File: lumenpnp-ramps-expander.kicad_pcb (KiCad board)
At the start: 2 copper layers, 53 x 98 mm, 70 parts, among them J1 12/24V, J10 A_MICROSTEPS, J11 A_DIAG, J12 A_VDD, J13 DIAG, J14 B_MICROSTEPS, J15 A_DIAG, J16 B_VDD, J2 EXP1, J3 EXP2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

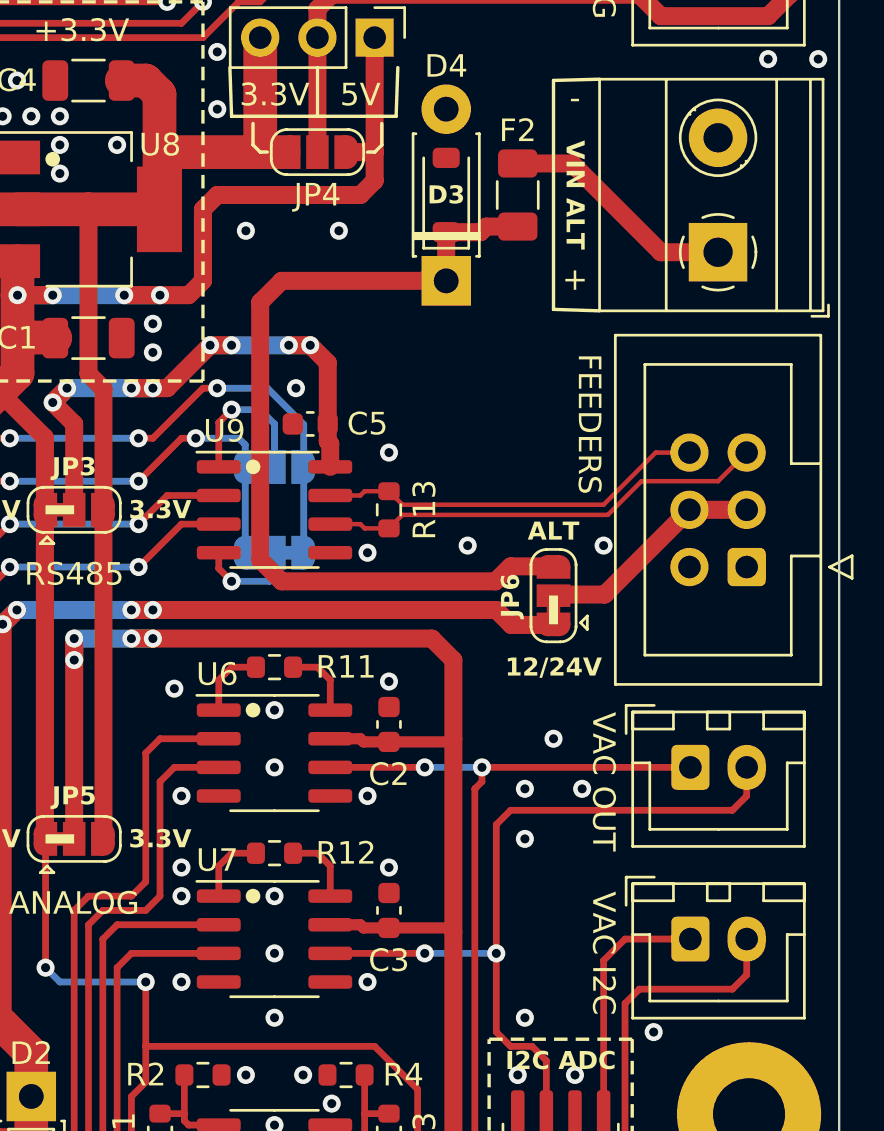
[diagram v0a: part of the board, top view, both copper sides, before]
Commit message: Add NIS4461 efuse for feeder power
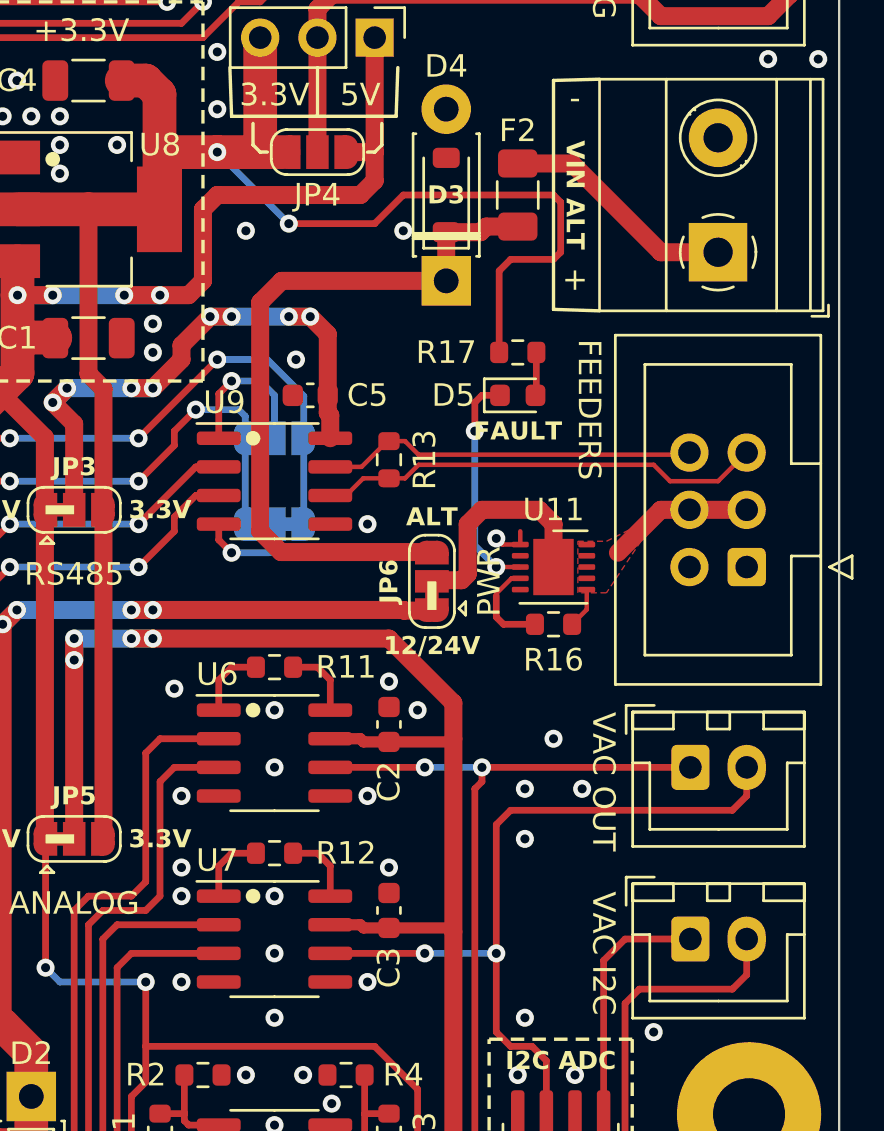
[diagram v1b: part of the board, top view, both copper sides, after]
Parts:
- added D5: FAULT, LED_SMD:LED_0603_1608Metric, F.Cu at (-31.3, 50.6)
- added R16: 20, Resistor_SMD:R_0603_1608Metric, F.Cu at (-29.7, 60.8)
- added R17: 470, Resistor_SMD:R_0603_1608Metric, F.Cu at (-31.3, 48.7)
- added U11: NIS4461, Package_DFN_QFN:WDFN-10-1EP_3x3mm_P0.5mm_EP1.8x2.5mm, F.Cu at (-29.7, 58.2)
- moved JP6 5.43 mm to (-35.1, 58.9)
- moved R13 2.22 mm to (-37.0, 53.5)
- moved C5 1.27 mm to (-40.5, 50.6)
- moved JP1 1.27 mm to (-42.1, 52.5)
- moved JP2 1.27 mm to (-42.1, 56.3)
- moved U9 1.27 mm to (-42.1, 54.4)
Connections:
- J7 pad 3: /VCC_FEEDERS -> Net-(J7-Pin_3)
- J7 pad 4: /VCC_FEEDERS -> Net-(J7-Pin_3)
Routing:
- net +3.3V: track 52.1 -> 78.2 mm, vias 0 -> 2
- net Net-(D5-K): track 0.00 -> 10.0 mm, vias 0 -> 2
- net Net-(J7-Pin_3): track 0.00 -> 8.31 mm
- net /VIN_ALT_FEEDERS: track 39.2 -> 32.3 mm
- net +VDC: track 181.7 -> 176.0 mm
- net Net-(U11-I_{LIMIT}): track 0.00 -> 4.24 mm
- net GND: track 16.5 -> 18.5 mm, vias 102 -> 101
- net Net-(D5-A): track 0.00 -> 1.92 mm
- net VDDA: track 92.1 -> 91.0 mm
- net /D17: track 38.4 -> 39.3 mm
- net /D49: track 31.3 -> 32.2 mm
- net /VCC_TRANSCEIVER: track 27.2 -> 28.1 mm
- net /RS-485-: track 17.2 -> 16.4 mm
- net /D16: track 39.7 -> 40.2 mm
- net /D33: track 30.8 -> 31.3 mm
- added copper zone on F.Cu, net Net-(J7-Pin_3)
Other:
- board text added: "FAULT"
- board text added: "PWR"
